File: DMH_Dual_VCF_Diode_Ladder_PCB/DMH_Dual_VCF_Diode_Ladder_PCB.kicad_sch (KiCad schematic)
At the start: 0 parts

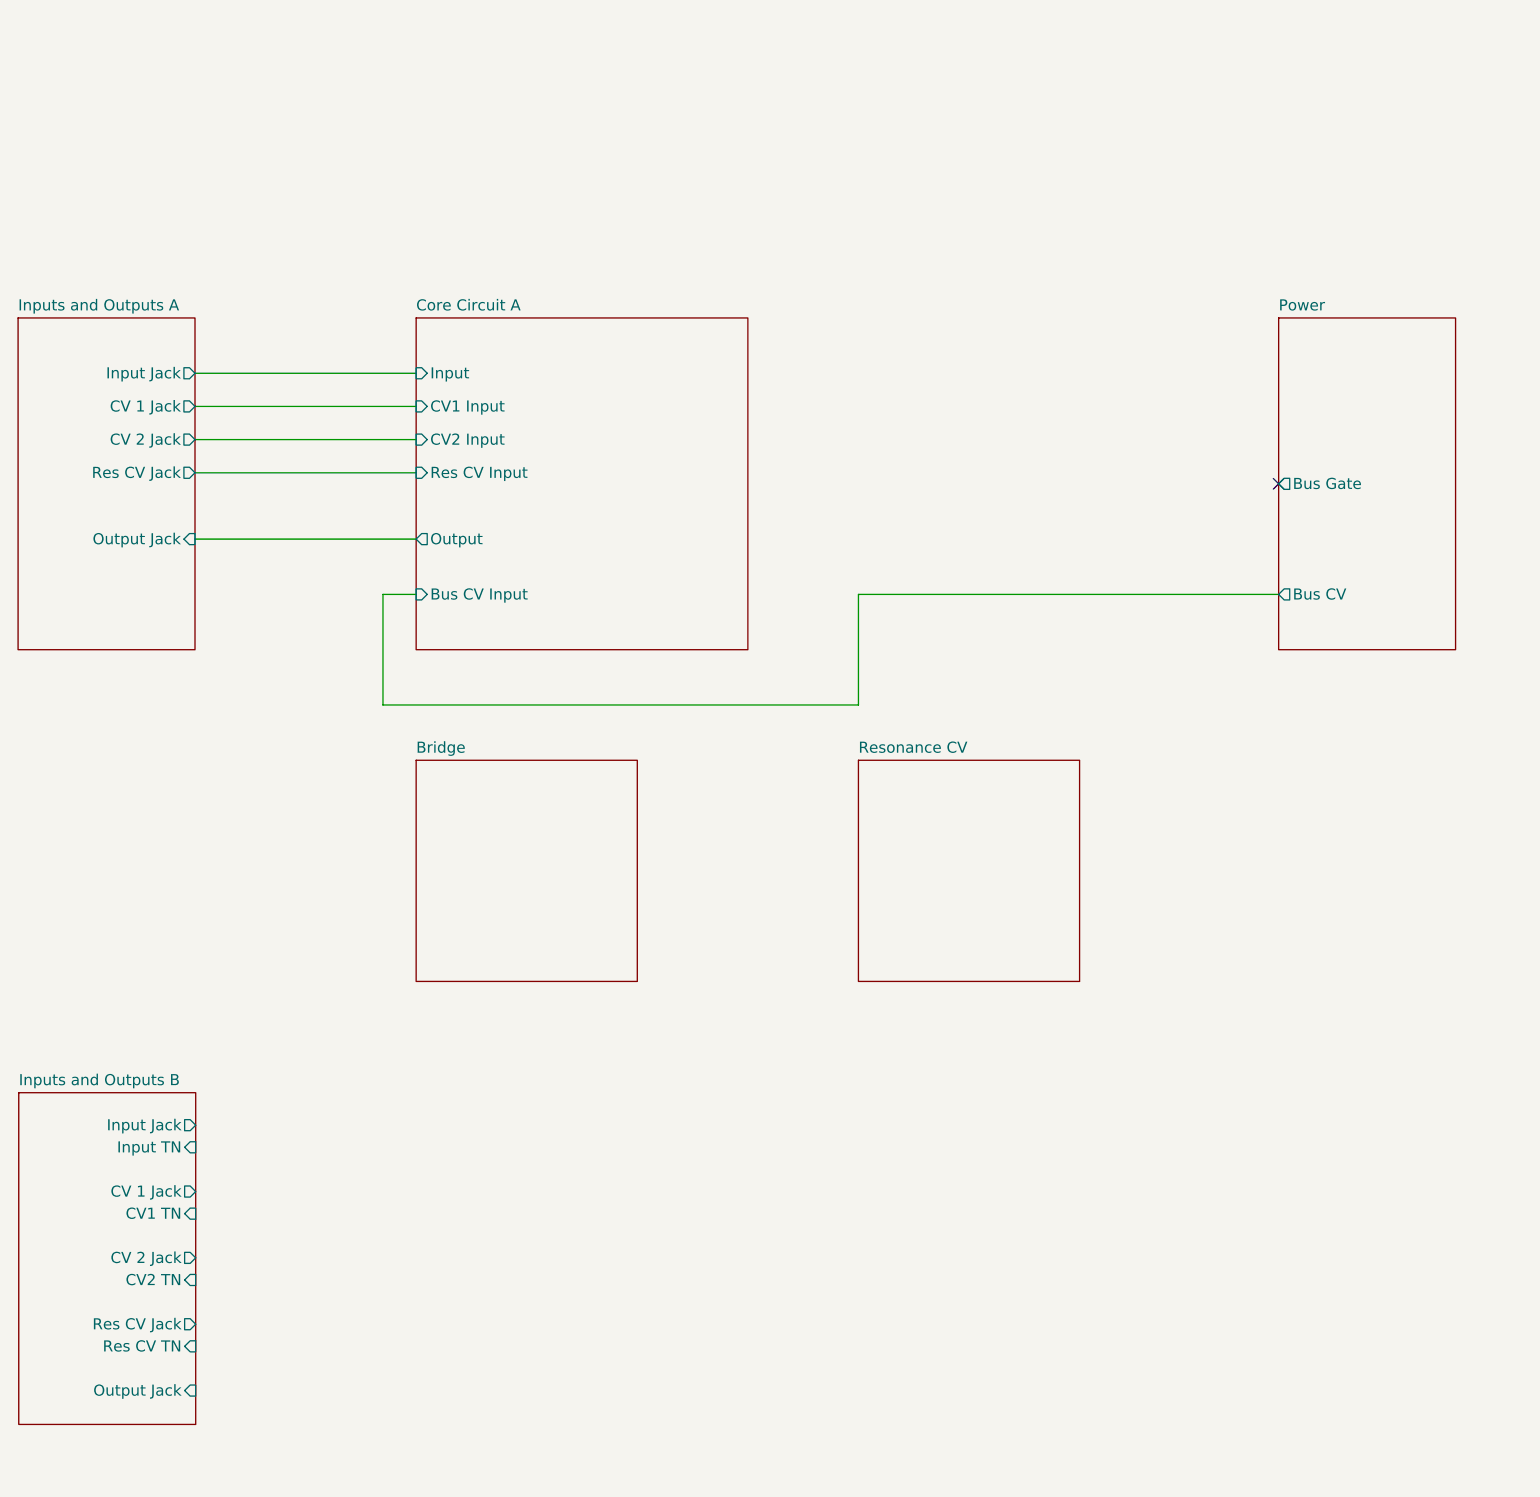
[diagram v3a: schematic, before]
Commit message: Concluded core and resonance circuits design
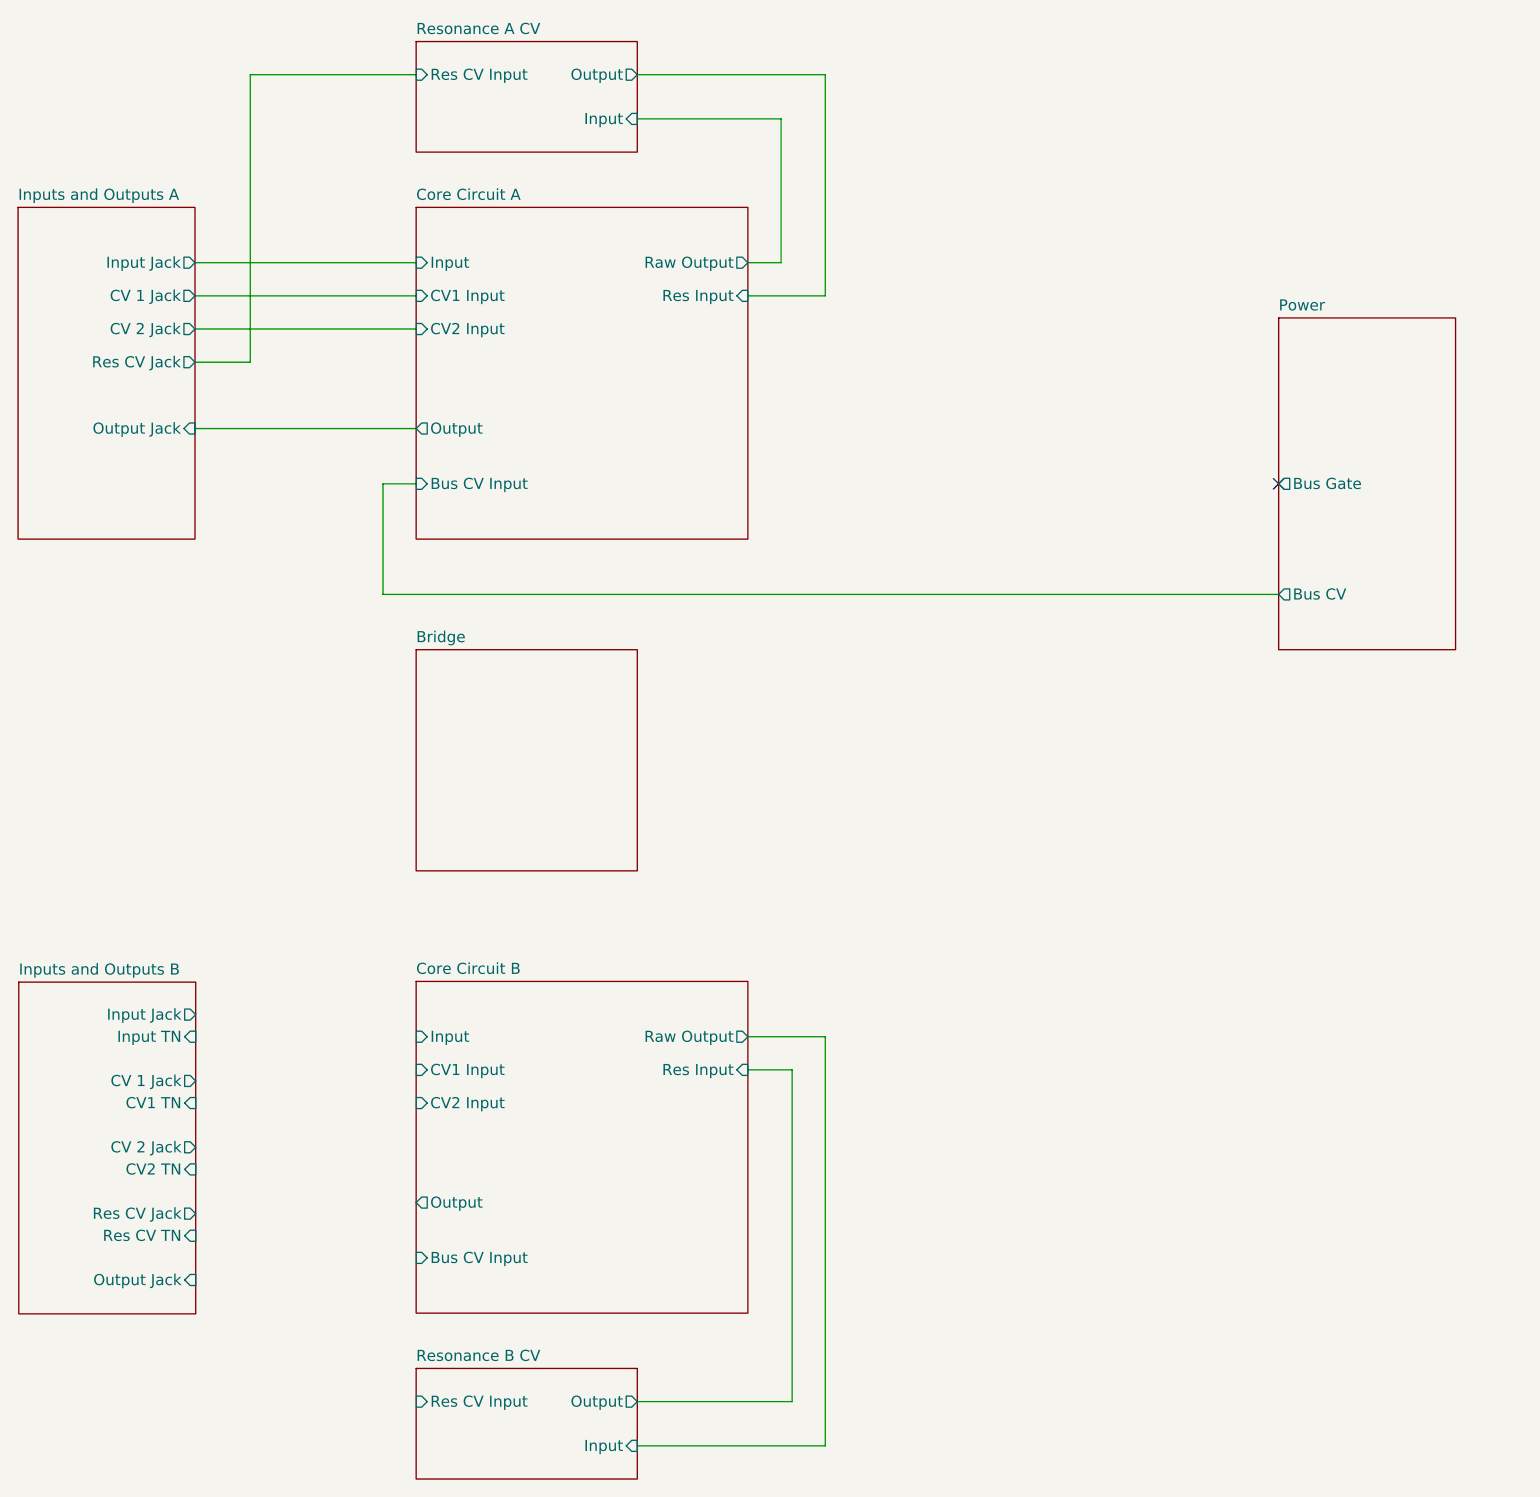
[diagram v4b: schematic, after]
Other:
- sheet Resonance CV renamed Resonance A CV
- added sheet Core Circuit B (Core_Circuit_B.kicad_sch)
- added sheet Resonance B CV (Resonance_B_CV.kicad_sch)
- sheet Core Circuit A ports: added Raw Output, Res Input; removed Res CV Input
- sheet Resonance A CV: file Resonance_CV.kicad_sch -> Resonance_A_CV.kicad_sch
- sheet Resonance A CV ports: added Input, Output, Res CV Input; removed none

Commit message: Added Bus CV buffering
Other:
- sheet Bridge renamed CV Processing
- sheet CV Processing: file Bridge.kicad_sch -> CV_Processing.kicad_sch
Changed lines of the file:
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@@
 			(color 0 0 0 0.0000)
 		)
-		(property "Sheetname" "Bridge"
+		(property "Sheetname" "CV Processing"
 			(at 63.5 88.1884 0)
 			(effects
@@
 			)
 		)
-		(property "Sheetfile" "Bridge.kicad_sch"
+		(property "Sheetfile" "CV_Processing.kicad_sch"
 			(at 63.5 114.8846 0)
 			(effects

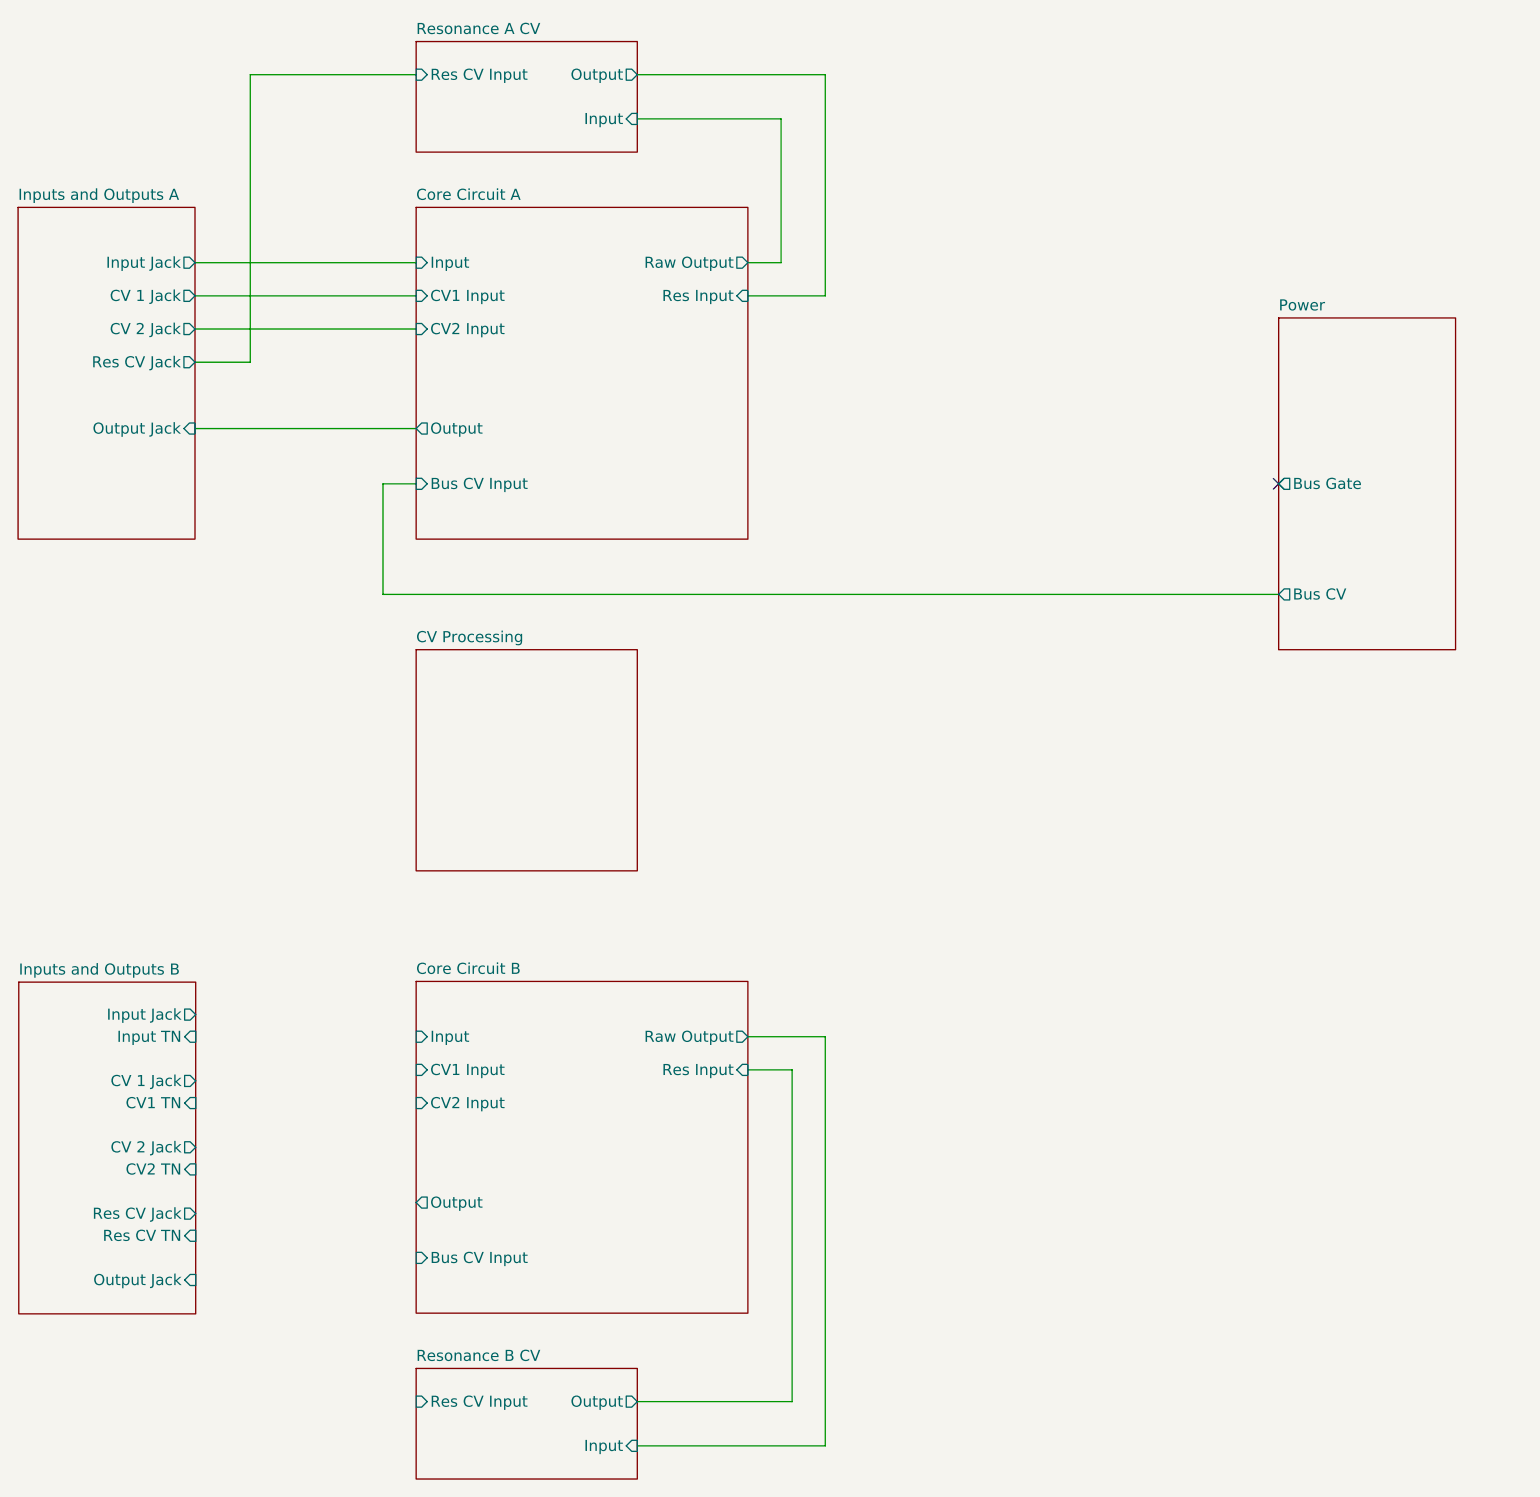
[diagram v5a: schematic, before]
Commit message: Made CV processing page
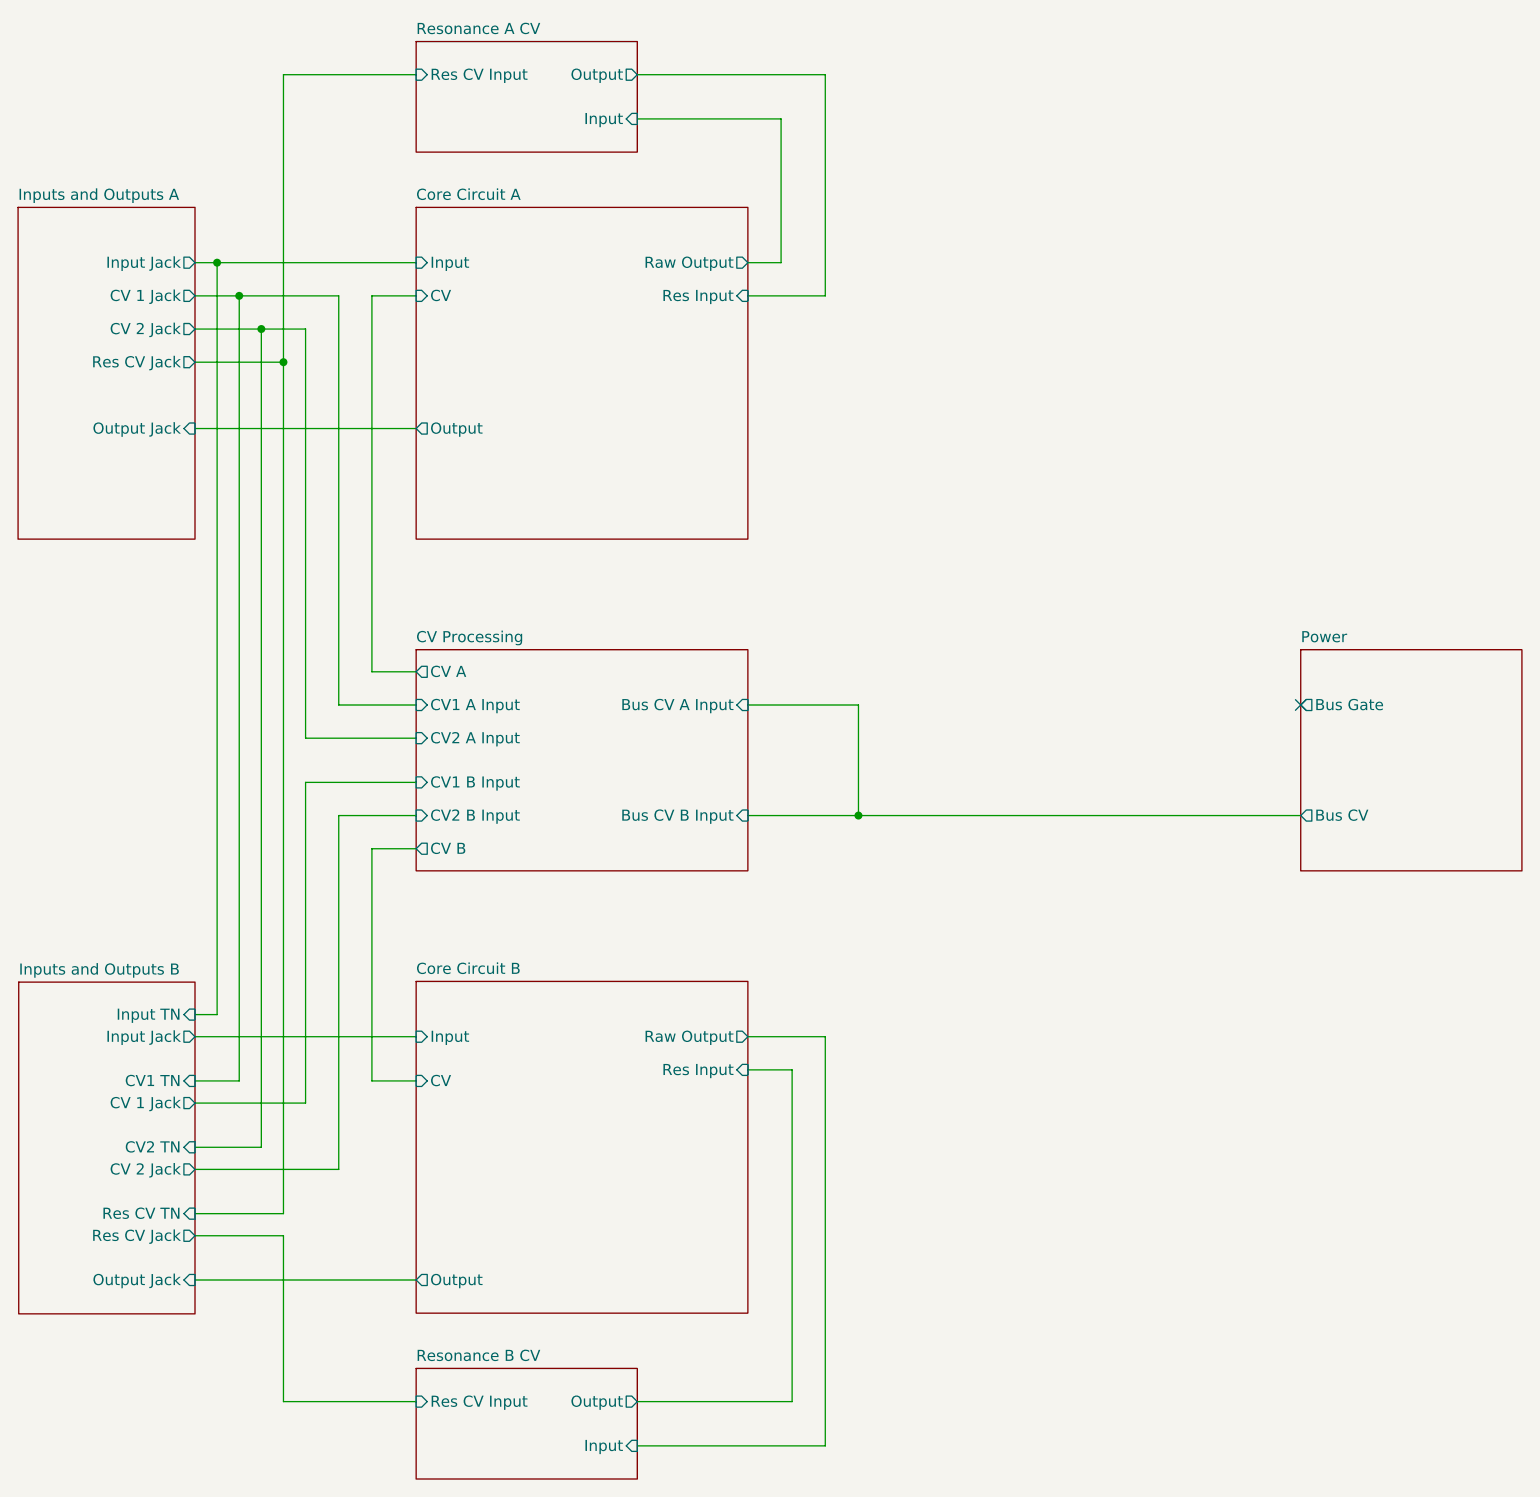
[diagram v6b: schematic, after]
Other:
- sheet CV Processing ports: added Bus CV A Input, Bus CV B Input, CV A, CV B, CV1 A Input, CV1 B Input, CV2 A Input, CV2 B Input; removed none
- sheet Core Circuit A ports: added CV; removed Bus CV Input, CV1 Input, CV2 Input
- sheet Core Circuit B ports: added CV; removed Bus CV Input, CV1 Input, CV2 Input

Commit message: Finished designing circuit
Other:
- sheet CV Processing ports: added Link Switch; removed CV B
- sheet Inputs and Outputs A ports: added Feed Switch; removed none
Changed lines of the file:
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@@
-	)
-	(junction
-		(at 40.64 44.45)
-		(diameter 0)
-		(color 0 0 0 0)
 	)
 	(junction
@@
 	(wire
 		(pts
+			(xy 38.1 130.81) (xy 40.64 130.81)
+		)
+		(stroke
+			(width 0)
+			(type default)
+		)
+	)
+	(wire
+		(pts
 			(xy 110.49 48.26) (xy 101.6 48.26)
 		)
@@
 	(wire
 		(pts
-			(xy 38.1 44.45) (xy 40.64 44.45)
+			(xy 38.1 44.45) (xy 63.5 44.45)
 		)
 		(stroke
@@
 	(wire
 		(pts
-			(xy 38.1 130.81) (xy 40.64 130.81)
-		)
-		(stroke
-			(width 0)
-			(type default)
-		)
-	)
-	(wire
-		(pts
 			(xy 63.5 111.76) (xy 58.42 111.76)
 		)
@@
 	(wire
 		(pts
-			(xy 40.64 44.45) (xy 63.5 44.45)
-		)
-		(stroke
-			(width 0)
-			(type default)
-		)
-	)
-	(wire
-		(pts
 			(xy 38.1 48.26) (xy 43.18 48.26)
 		)
@@
 	(wire
 		(pts
+			(xy 40.64 71.12) (xy 38.1 71.12)
+		)
+		(stroke
+			(width 0)
+			(type default)
+		)
+	)
+	(wire
+		(pts
 			(xy 101.6 107.95) (xy 114.3 107.95)
 		)
@@
 	(wire
 		(pts
-			(xy 40.64 130.81) (xy 40.64 44.45)
-		)
-		(stroke
-			(width 0)
-			(type default)
-		)
-	)
-	(wire
-		(pts
 			(xy 48.26 153.67) (xy 48.26 55.88)
 		)
@@
 		(pts
 			(xy 48.26 175.26) (xy 63.5 175.26)
+		)
+		(stroke
+			(width 0)
+			(type default)
+		)
+	)
+	(wire
+		(pts
+			(xy 40.64 130.81) (xy 40.64 71.12)
 		)
 		(stroke
@@
 			(project "DMH_Dual_VCF_Diode_Ladder_PCB"
 				(path "/58f4306d-5387-4983-bb08-41a2313fd315"
-					(page "9")
+					(page "8")
 				)
 			)
@@
 			)
 		)
+		(pin "Feed Switch" output
+			(at 38.1 71.12 0)
+			(effects
+				(font
+					(size 1.27 1.27)
+				)
+				(justify right)
+			)
+		)
 		(instances
 			(project "DMH_Dual_VCF_Diode_Ladder_PCB"
@@
 			)
 		)
-		(pin "CV B" output
+		(pin "Link Switch" output
 			(at 63.5 111.76 180)
 			(effects
@@
 			(project "DMH_Dual_VCF_Diode_Ladder_PCB"
 				(path "/58f4306d-5387-4983-bb08-41a2313fd315"
-					(page "8")
-				)
-			)
+					(page "9")
+				)
+			)
